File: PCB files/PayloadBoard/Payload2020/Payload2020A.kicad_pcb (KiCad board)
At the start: 2 copper layers, 31.8 x 152.4 mm, 28 parts, among them J1 BATTERY, J2 BridgeConn, J3 LoadCell, Q1 Q_NMOS_GSD, Q2 Q_NMOS_GSD, SW1 SW_SPST, U1 Teensy3.6, U2 ArduCam, U3 HX711_Breakout, U4 AP7370-50W5-7, U5 TPS613222ADBVR

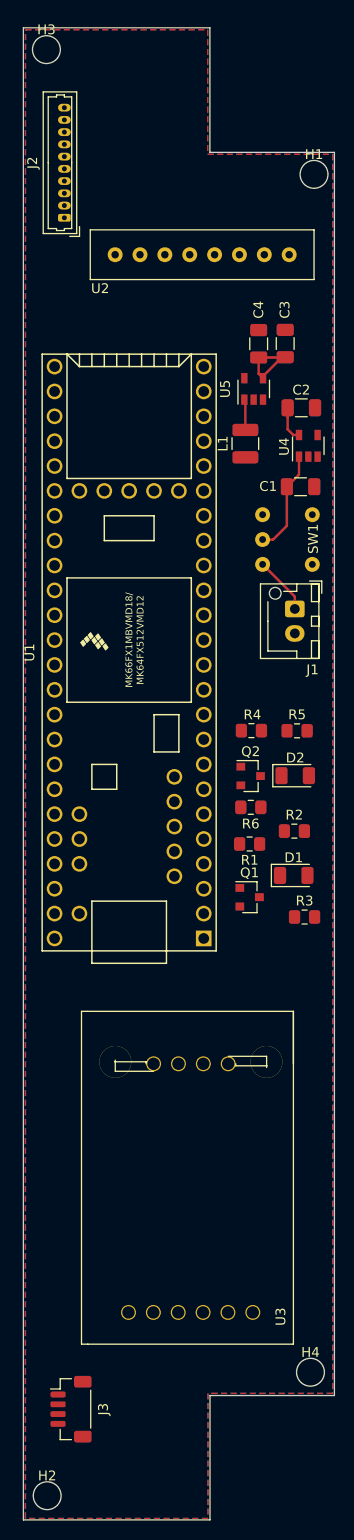
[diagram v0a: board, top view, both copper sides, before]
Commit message: BIG changus -Fully routed both boards -Changed board to board connector to JST SH -Changed load cell connector to molex picoblade -Added silkscreen version & signature -Moved arducam connector to align with payload structure
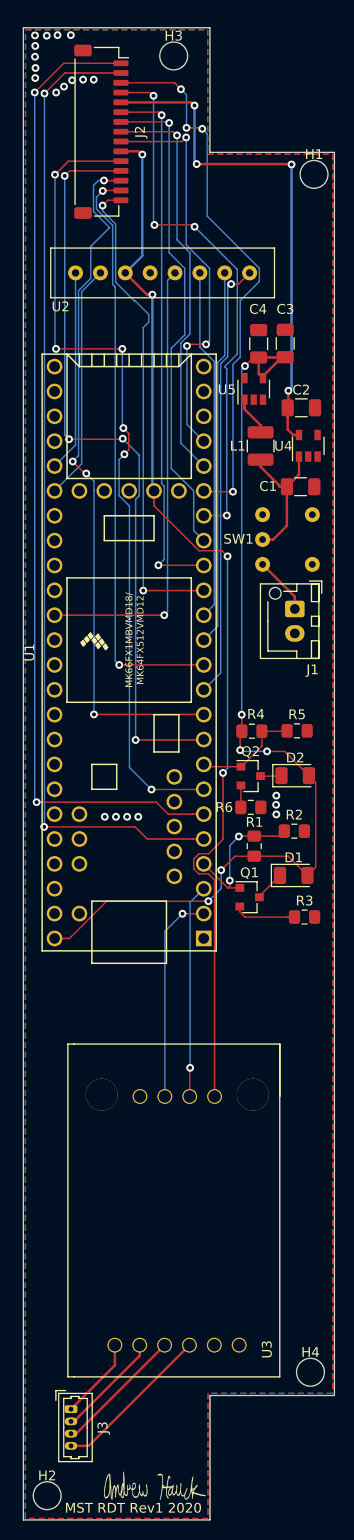
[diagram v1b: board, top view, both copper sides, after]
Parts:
- added G***: LOGO, Board images:AAHsig, F.Cu at (133.8, 169.7)
- J2: footprint Connector_Molex:Molex_PicoBlade_53047-1010_1x10_P1.25mm_Vertical -> Connector_JST:JST_SH_SM15B-SRSS-TB_1x15-1MP_P1.00mm_Horizontal
- J3: footprint Connector_JST:JST_SH_BM04B-SRSS-TB_1x04-1MP_P1.00mm_Vertical -> Connector_Molex:Molex_PicoBlade_53047-0410_1x04_P1.25mm_Vertical
- moved H3 13.0 mm to (135.8, 23.4)
- moved J2 9.57 mm to (128.4, 31.2), turned to 270 degrees
- moved U2 4.45 mm to (134.7, 45.3)
- moved U3 3.62 mm to (136.2, 143.0)
- moved L1 1.58 mm to (144.7, 63.3)
- moved R1 0.52 mm to (144.0, 104.1), turned to 90 degrees
- moved R4 0.08 mm to (143.8, 92.4), turned to 0 degrees
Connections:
- U1 pad 10: Net-(U1-Pad10) -> /DRDY_G
- U1 pad 12: Net-(U1-Pad12) -> /INT1_XM
- U1 pad 15: Net-(U1-Pad15) -> /INT2_XM
- U1 pad 7: Net-(U1-Pad7) -> /DEN_G
- U1 pad 9: Net-(U1-Pad9) -> /INT_G
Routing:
- net +3V3: track 0.00 -> 108.8 mm, vias 0 -> 4
- net /Berry_SCL: track 0.00 -> 100.4 mm, vias 0 -> 2
- net /Berry_SDA: track 0.00 -> 100.2 mm, vias 0 -> 2
- net +5V: track 8.29 -> 99.7 mm, vias 0 -> 6
- net /DEN_G: track 0.00 -> 84.3 mm, vias 0 -> 6
- net /INT_G: track 0.00 -> 77.2 mm, vias 0 -> 4
- net /DRDY_G: track 0.00 -> 71.5 mm, vias 0 -> 4
- net /INT1_XM: track 0.00 -> 60.2 mm, vias 0 -> 2
- net /RX_GPS: track 0.00 -> 55.9 mm, vias 0 -> 4
- net /XBEE_RTS: track 0.00 -> 55.2 mm, vias 0 -> 2
- net /TX_GPS: track 0.00 -> 55.2 mm, vias 0 -> 4
- net /XBEE_CTS: track 0.00 -> 50.2 mm, vias 0 -> 1
- net /INT2_XM: track 0.00 -> 49.9 mm, vias 0 -> 2
- net +3.3VA: track 3.60 -> 52.1 mm, vias 0 -> 4
- net /Ardu_SCK: track 0.00 -> 46.6 mm, vias 0 -> 1
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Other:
- net class Default: clearance 0.2 -> 0.1524
- rule trace_clearance: 0.2 -> 0.1524
- rule trace_min: 0.2 -> 0.13
- rule via_min_size: 0.4 -> 0.6
- board text added: "BACK - Vertical FRONT - Horizontal"
- board text added: "MST RDT Rev1 2020"
- board text removed: "BACK - Horizontal FRONT - Vertical"
